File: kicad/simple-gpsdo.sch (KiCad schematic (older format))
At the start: 109 parts, among them J1 PPS_OUT, J10 FAN, J2 PWR, J3 ISP, J4 GPS_NEO, J5 GPS_IN, J6 10MHz_OUT, J7 NEO-6M, J8 10MHz_OUT, J9 USB_C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

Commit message: finalizing revC updates
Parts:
- removed C36: 22uF, Capacitor_SMD:C_1206_3216Metric_Pad1.42x1.75mm_HandSolder, symbol Device:CP_Small
- removed C37: 0.1uF, Capacitor_SMD:C_0805_2012Metric_Pad1.15x1.40mm_HandSolder, symbol Device:C_Small
- removed D6: 1N4148, Diode_SMD:D_SOD-123, symbol Device:D_Small
- removed J10: FAN, Connector_PinHeader_2.54mm:PinHeader_1x02_P2.54mm_Vertical, symbol Connector:Conn_01x02_Female
- removed L4: 3.3uH, Inductor_SMD:L_1206_3216Metric_Pad1.42x1.75mm_HandSolder, symbol Device:L_Small
- removed Q2: PMBT2222, Package_TO_SOT_SMD:SOT-23_Handsoldering, symbol Device:Q_NPN_BEC
- removed R30: 1k, Resistor_SMD:R_0805_2012Metric_Pad1.15x1.40mm_HandSolder, symbol Device:R_Small
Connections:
- net labels removed: FAN_PWM
- wire segments 285 -> 273
- no-connect marks 20 -> 21
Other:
- note removed: "Fan Control"
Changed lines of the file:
@@
 Wire Wire Line
 	7800 4000 7750 4000
-Text Label 4550 5100 1    50   ~ 0
-ADC2
 $Comp
 L Device:R_Small R28
@@
 Text Label 4600 4200 0    50   ~ 0
 ADC2
-$Comp
-L Device:Q_NPN_BEC Q2
-U 1 1 5F768340
-P 1600 7350
-F 0 "Q2" H 1791 7396 50  0000 L CNN
-F 1 "PMBT2222" H 1791 7305 50  0000 L CNN
-F 2 "Package_TO_SOT_SMD:SOT-23_Handsoldering" H 1800 7450 50  0001 C CNN
-F 3 "~" H 1600 7350 50  0001 C CNN
-	1    1600 7350
-	-1   0    0    -1
-$EndComp
-$Comp
-L Device:D_Small D6
-U 1 1 5F785CB2
-P 1500 6950
-F 0 "D6" V 1454 7020 50  0000 L CNN
-F 1 "1N4148" V 1545 7020 50  0000 L CNN
-F 2 "Diode_SMD:D_SOD-123" V 1500 6950 50  0001 C CNN
-F 3 "~" V 1500 6950 50  0001 C CNN
-	1    1500 6950
-	0    1    1    0
-$EndComp
-$Comp
-L Connector:Conn_01x02_Female J10
-U 1 1 5F786D71
-P 1000 7000
-F 0 "J10" H 892 7185 50  0000 C CNN
-F 1 "FAN" H 892 7094 50  0000 C CNN
-F 2 "Connector_PinHeader_2.54mm:PinHeader_1x02_P2.54mm_Vertical" H 1000 7000 50  0001 C CNN
-F 3 "~" H 1000 7000 50  0001 C CNN
-	1    1000 7000
-	-1   0    0    -1
-$EndComp
-$Comp
-L power:GND #PWR066
-U 1 1 5F78873A
-P 1500 7550
-F 0 "#PWR066" H 1500 7300 50  0001 C CNN
-F 1 "GND" H 1505 7377 50  0001 C CNN
-F 2 "" H 1500 7550 50  0001 C CNN
-F 3 "" H 1500 7550 50  0001 C CNN
-	1    1500 7550
-	1    0    0    -1
-$EndComp
-$Comp
-L Device:R_Small R30
-U 1 1 5F78892D
-P 1900 7350
-F 0 "R30" V 2000 7350 50  0000 C BNN
-F 1 "1k" V 1900 7350 40  0000 C CNN
-F 2 "Resistor_SMD:R_0805_2012Metric_Pad1.15x1.40mm_HandSolder" H 1900 7350 50  0001 C CNN
-F 3 "~" H 1900 7350 50  0001 C CNN
-	1    1900 7350
-	0    1    1    0
-$EndComp
-Text GLabel 2100 7450 3    40   Input ~ 0
-FAN_PWM
-Wire Wire Line
-	2100 7350 2000 7350
-$Comp
-L Device:CP_Small C36
-U 1 1 5F7F8DFC
-P 1800 6850
-F 0 "C36" H 1888 6896 50  0000 L CNN
-F 1 "22uF" H 1888 6805 50  0000 L CNN
-F 2 "Capacitor_SMD:C_1206_3216Metric_Pad1.42x1.75mm_HandSolder" H 1800 6850 50  0001 C CNN
-F 3 "~" H 1800 6850 50  0001 C CNN
-	1    1800 6850
-	1    0    0    -1
-$EndComp
-Wire Wire Line
-	2100 7350 2100 7450
-$Comp
-L power:GND #PWR067
-U 1 1 5F8108C5
-P 1800 6950
-F 0 "#PWR067" H 1800 6700 50  0001 C CNN
-F 1 "GND" H 1805 6777 50  0001 C CNN
-F 2 "" H 1800 6950 50  0001 C CNN
-F 3 "" H 1800 6950 50  0001 C CNN
-	1    1800 6950
-	1    0    0    -1
-$EndComp
-$Comp
-L Device:C_Small C37
-U 1 1 5F810BCA
-P 2150 6850
-F 0 "C37" V 1921 6850 50  0000 C CNN
-F 1 "0.1uF" V 2012 6850 50  0000 C CNN
-F 2 "Capacitor_SMD:C_0805_2012Metric_Pad1.15x1.40mm_HandSolder" H 2150 6850 50  0001 C CNN
-F 3 "~" H 2150 6850 50  0001 C CNN
-	1    2150 6850
-	-1   0    0    -1
-$EndComp
-$Comp
-L power:GND #PWR068
-U 1 1 5F81112D
-P 2150 6950
-F 0 "#PWR068" H 2150 6700 50  0001 C CNN
-F 1 "GND" H 2155 6777 50  0001 C CNN
-F 2 "" H 2150 6950 50  0001 C CNN
-F 3 "" H 2150 6950 50  0001 C CNN
-	1    2150 6950
-	1    0    0    -1
-$EndComp
-Wire Wire Line
-	1200 7000 1350 7000
-Wire Wire Line
-	2150 6700 2150 6750
-$Comp
-L power:+5VD #PWR065
-U 1 1 5F858FD4
-P 1350 6450
-F 0 "#PWR065" H 1350 6300 50  0001 C CNN
-F 1 "+5VD" H 1365 6623 50  0000 C CNN
-F 2 "" H 1350 6450 50  0001 C CNN
-F 3 "" H 1350 6450 50  0001 C CNN
-	1    1350 6450
-	1    0    0    -1
-$EndComp
-$Comp
-L Device:L_Small L4
-U 1 1 5F859F8F
-P 1350 6550
-F 0 "L4" H 1398 6596 50  0000 L CNN
-F 1 "3.3uH" H 1398 6505 50  0000 L CNN
-F 2 "Inductor_SMD:L_1206_3216Metric_Pad1.42x1.75mm_HandSolder" H 1350 6550 50  0001 C CNN
-F 3 "~" H 1350 6550 50  0001 C CNN
-	1    1350 6550
-	-1   0    0    -1
-$EndComp
-Wire Wire Line
-	2150 6700 1800 6700
-Wire Wire Line
-	1500 6850 1500 6700
-Wire Wire Line
-	1800 6750 1800 6700
-Connection ~ 1800 6700
-Wire Wire Line
-	1800 6700 1500 6700
-Wire Wire Line
-	1350 6650 1350 7000
-Wire Wire Line
-	1500 7050 1500 7100
-Wire Wire Line
-	1200 7100 1500 7100
-Connection ~ 1500 7100
-Wire Wire Line
-	1500 7100 1500 7150
-Text Notes 1500 6600 0    50   ~ 0
-Fan Control
-Text GLabel 2650 4850 3    40   Input ~ 0
-FAN_PWM
-Text GLabel 4100 3400 2    50   Input ~ 0
-FAN_PWM
+NoConn ~ 4100 3400
 $EndSCHEMATC

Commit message: schematic cleanup and re-plot of gerber files
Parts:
- J9: symbol Connector:USB_C_Receptacle_USB2.0 -> simple-gpsdo-rescue:USB_C_Receptacle_USB2.0-Connector
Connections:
- no-connect marks 21 -> 20
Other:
- moved on the sheet: C1, C2, Y1
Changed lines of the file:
@@
 Connection ~ 2800 1150
-$Comp
-L Device:C_Small C2
-U 1 1 5F6D722A
-P 2250 3950
-F 0 "C2" H 2158 3904 50  0000 R CNN
-F 1 "6.8pF" H 2158 3995 50  0000 R CNN
-F 2 "Capacitor_SMD:C_0805_2012Metric_Pad1.15x1.40mm_HandSolder" H 2250 3950 50  0001 C CNN
-F 3 "~" H 2250 3950 50  0001 C CNN
-	1    2250 3950
-	0    -1   -1   0
-$EndComp
-$Comp
-L Device:C_Small C1
-U 1 1 5F6DDEED
-P 2250 3450
-F 0 "C1" H 2159 3404 50  0000 R CNN
-F 1 "6.8pF" H 2159 3495 50  0000 R CNN
-F 2 "Capacitor_SMD:C_0805_2012Metric_Pad1.15x1.40mm_HandSolder" H 2250 3450 50  0001 C CNN
-F 3 "~" H 2250 3450 50  0001 C CNN
-	1    2250 3450
-	0    -1   1    0
-$EndComp
 $Comp
 L Device:C_Small C4
@@
 F 3 "~" H 1550 1250 50  0001 C CNN
 	1    1550 1250
-	1    0    0    -1
+	-1   0    0    -1
 $EndComp
 Wire Wire Line
@@
 $EndComp
 $Comp
-L Connector:USB_C_Receptacle_USB2.0 J9
+L simple-gpsdo-rescue:USB_C_Receptacle_USB2.0-Connector J9
 U 1 1 5F73B888
 P 1300 2600
@@
 NoConn ~ 1900 2300
 NoConn ~ 2850 2150
-NoConn ~ 1250 800
-$Comp
-L Device:Crystal_GND24 Y1
-U 1 1 5F750A50
-P 2400 3700
-F 0 "Y1" V 2150 3600 50  0000 R CNN
-F 1 "16MHz" V 2250 3600 50  0000 R CNN
-F 2 "Crystal:Crystal_SMD_SeikoEpson_TSX3225-4Pin_3.2x2.5mm_HandSoldering" H 2400 3700 50  0001 C CNN
-F 3 "~" H 2400 3700 50  0001 C CNN
-	1    2400 3700
-	0    -1   1    0
-$EndComp
 Wire Wire Line
 	1600 3950 1600 3850
@@
 	1    0    0    -1
 $EndComp
-$Comp
-L power:GND #PWR03
-U 1 1 5F85D4E9
-P 2100 4050
-F 0 "#PWR03" H 2100 3800 50  0001 C CNN
-F 1 "GND" H 2105 3877 50  0001 C CNN
-F 2 "" H 2100 4050 50  0001 C CNN
-F 3 "" H 2100 4050 50  0001 C CNN
-	1    2100 4050
-	1    0    0    -1
-$EndComp
-$Comp
-L power:GND #PWR07
-U 1 1 5F85DF21
-P 2650 3750
-F 0 "#PWR07" H 2650 3500 50  0001 C CNN
-F 1 "GND" H 2655 3577 50  0001 C CNN
-F 2 "" H 2650 3750 50  0001 C CNN
-F 3 "" H 2650 3750 50  0001 C CNN
-	1    2650 3750
-	1    0    0    -1
-$EndComp
-Wire Wire Line
-	2600 3700 2650 3700
-Wire Wire Line
-	2500 3700 2500 3750
-Wire Wire Line
-	2350 3450 2400 3450
-Wire Wire Line
-	2400 3450 2400 3550
-Wire Wire Line
-	2150 3450 2100 3450
-Wire Wire Line
-	2100 3450 2100 3700
-Wire Wire Line
-	2150 3950 2100 3950
-Connection ~ 2100 3950
-Wire Wire Line
-	2100 3950 2100 4050
-Wire Wire Line
-	2200 3700 2100 3700
-Connection ~ 2100 3700
-Wire Wire Line
-	2100 3700 2100 3950
-Wire Wire Line
-	2350 3950 2400 3950
-Wire Wire Line
-	2400 3950 2400 3850
 Text GLabel 2700 1700 0    50   Input ~ 0
 XTAL1
@@
 Wire Wire Line
 	2700 1900 2900 1900
-Text GLabel 2400 3350 1    50   Input ~ 0
-XTAL1
-Wire Wire Line
-	2400 3350 2400 3450
-Connection ~ 2400 3450
-Text GLabel 2400 4050 3    50   Input ~ 0
-XTAL2
-Wire Wire Line
-	2400 3950 2400 4050
-Connection ~ 2400 3950
-Wire Wire Line
-	2650 3750 2650 3700
+Wire Wire Line
+	2850 4000 2850 3950
 Wire Wire Line
 	4100 2200 4900 2200
@@
 ADC2
 NoConn ~ 4100 3400
+Connection ~ 2600 4200
+Wire Wire Line
+	2600 4200 2600 4300
+Text GLabel 2600 4300 3    50   Input ~ 0
+XTAL2
+Connection ~ 2600 3700
+Wire Wire Line
+	2600 3600 2600 3700
+Text GLabel 2600 3600 1    50   Input ~ 0
+XTAL1
+Wire Wire Line
+	2600 4200 2600 4100
+Wire Wire Line
+	2550 4200 2600 4200
+Wire Wire Line
+	2300 3950 2300 4200
+Connection ~ 2300 3950
+Wire Wire Line
+	2400 3950 2300 3950
+Wire Wire Line
+	2300 4200 2300 4300
+Connection ~ 2300 4200
+Wire Wire Line
+	2350 4200 2300 4200
+Wire Wire Line
+	2300 3700 2300 3950
+Wire Wire Line
+	2350 3700 2300 3700
+Wire Wire Line
+	2600 3700 2600 3800
+Wire Wire Line
+	2550 3700 2600 3700
+Wire Wire Line
+	2700 3950 2700 4000
+Wire Wire Line
+	2800 3950 2850 3950
+$Comp
+L power:GND #PWR07
+U 1 1 5F85DF21
+P 2850 4000
+F 0 "#PWR07" H 2850 3750 50  0001 C CNN
+F 1 "GND" H 2855 3827 50  0001 C CNN
+F 2 "" H 2850 4000 50  0001 C CNN
+F 3 "" H 2850 4000 50  0001 C CNN
+	1    2850 4000
+	1    0    0    -1
+$EndComp
+$Comp
+L power:GND #PWR03
+U 1 1 5F85D4E9
+P 2300 4300
+F 0 "#PWR03" H 2300 4050 50  0001 C CNN
+F 1 "GND" H 2305 4127 50  0001 C CNN
+F 2 "" H 2300 4300 50  0001 C CNN
+F 3 "" H 2300 4300 50  0001 C CNN
+	1    2300 4300
+	1    0    0    -1
+$EndComp
+$Comp
+L Device:Crystal_GND24 Y1
+U 1 1 5F750A50
+P 2600 3950
+F 0 "Y1" V 2350 3850 50  0000 R CNN
+F 1 "16MHz" V 2450 3850 50  0000 R CNN
+F 2 "Crystal:Crystal_SMD_SeikoEpson_TSX3225-4Pin_3.2x2.5mm_HandSoldering" H 2600 3950 50  0001 C CNN
+F 3 "~" H 2600 3950 50  0001 C CNN
+	1    2600 3950
+	0    -1   1    0
+$EndComp
+$Comp
+L Device:C_Small C1
+U 1 1 5F6DDEED
+P 2450 3700
+F 0 "C1" H 2359 3654 50  0000 R CNN
+F 1 "6.8pF" H 2359 3745 50  0000 R CNN
+F 2 "Capacitor_SMD:C_0805_2012Metric_Pad1.15x1.40mm_HandSolder" H 2450 3700 50  0001 C CNN
+F 3 "~" H 2450 3700 50  0001 C CNN
+	1    2450 3700
+	0    -1   1    0
+$EndComp
+$Comp
+L Device:C_Small C2
+U 1 1 5F6D722A
+P 2450 4200
+F 0 "C2" H 2358 4154 50  0000 R CNN
+F 1 "6.8pF" H 2358 4245 50  0000 R CNN
+F 2 "Capacitor_SMD:C_0805_2012Metric_Pad1.15x1.40mm_HandSolder" H 2450 4200 50  0001 C CNN
+F 3 "~" H 2450 4200 50  0001 C CNN
+	1    2450 4200
+	0    -1   -1   0
+$EndComp
 $EndSCHEMATC

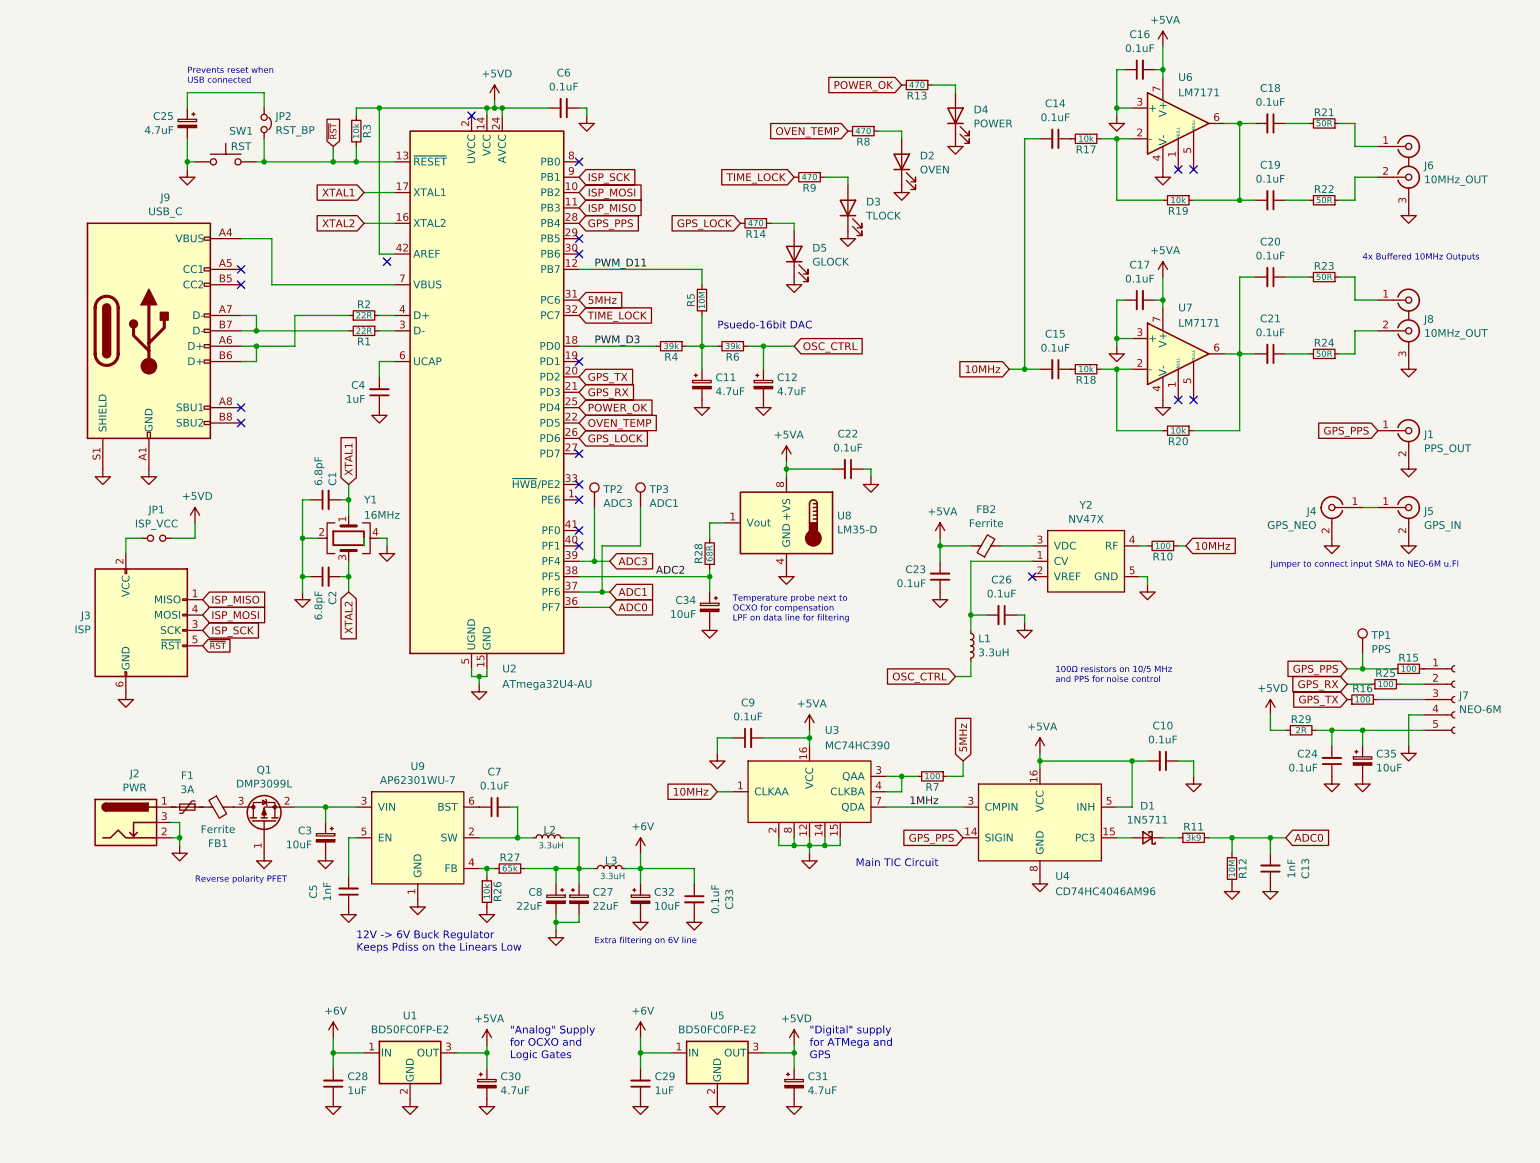
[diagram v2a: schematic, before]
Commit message: finalized simple schematic, started PCB rework
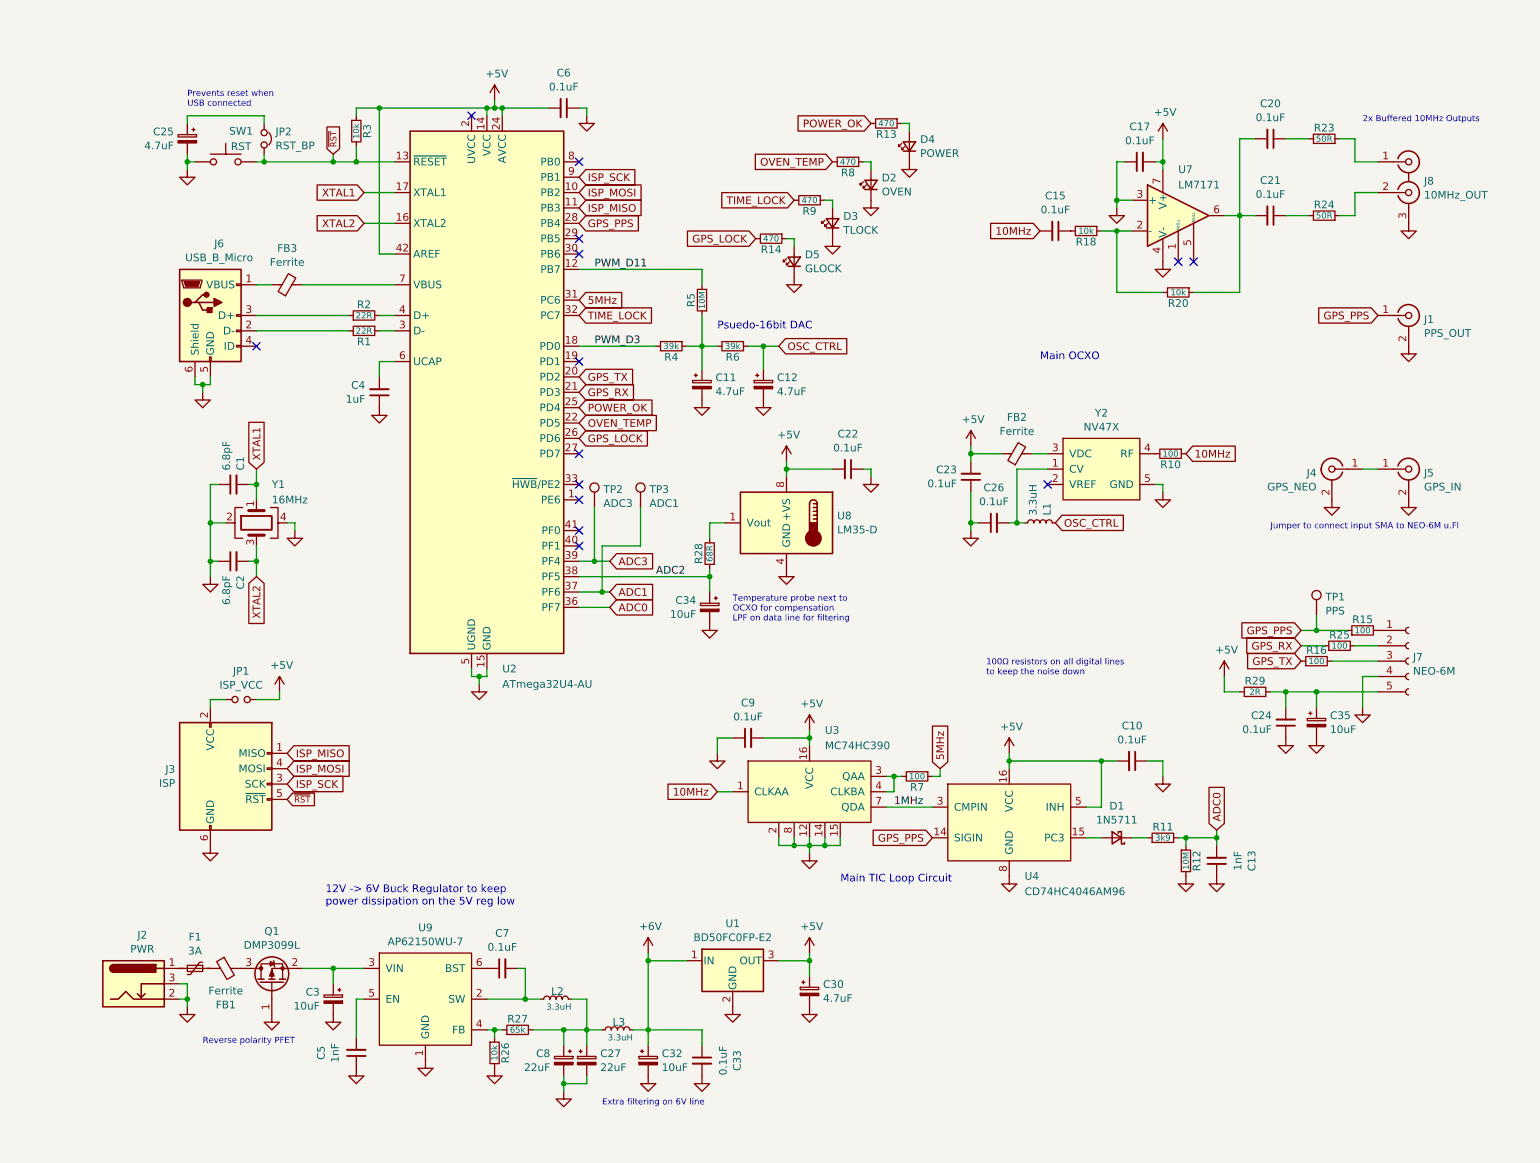
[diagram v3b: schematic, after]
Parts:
- removed C14, C16, C18, C19: 0.1uF, Capacitor_SMD:C_0805_2012Metric_Pad1.15x1.40mm_HandSolder, symbol Device:C_Small
- removed C28, C29: 1uF, Capacitor_SMD:C_0805_2012Metric_Pad1.15x1.40mm_HandSolder, symbol Device:C_Small
- removed C31: 4.7uF, Capacitor_SMD:C_1206_3216Metric_Pad1.42x1.75mm_HandSolder, symbol Device:CP_Small
- removed D2: OVEN, LED_SMD:LED_1206_3216Metric_Pad1.42x1.75mm_HandSolder, symbol Device:LED
- removed D3: TLOCK, LED_SMD:LED_1206_3216Metric_Pad1.42x1.75mm_HandSolder, symbol Device:LED
- removed D4: POWER, LED_SMD:LED_1206_3216Metric_Pad1.42x1.75mm_HandSolder, symbol Device:LED
- removed D5: GLOCK, LED_SMD:LED_1206_3216Metric_Pad1.42x1.75mm_HandSolder, symbol Device:LED
- removed J6: 10MHz_OUT, molex:734152980, symbol Connector:Conn_Coaxial_x2
- removed J9: USB_C, Kycon:KUSBX-SL-CS1N14-B, symbol simple-gpsdo-rescue:USB_C_Receptacle_USB2.0-Connector
- removed R17, R19: 10k, Resistor_SMD:R_0805_2012Metric_Pad1.15x1.40mm_HandSolder, symbol Device:R_Small
- removed R21, R22: 50R, Resistor_SMD:R_0805_2012Metric_Pad1.15x1.40mm_HandSolder, symbol Device:R_Small
- removed U5: BD50FC0FP-E2, Package_TO_SOT_SMD:TO-252-2, symbol Regulator_Linear:L7805
- removed U6: LM7171, Package_SO:SOIC-8_3.9x4.9mm_P1.27mm, symbol Amplifier_Operational:AD8610
- added D2: OVEN, LED_THT:LED_D3.0mm_Horizontal_O1.27mm_Z2.0mm_Clear, symbol Device:LED_Small
- added D3: TLOCK, LED_THT:LED_D3.0mm_Horizontal_O1.27mm_Z2.0mm_Clear, symbol Device:LED_Small
- added D4: POWER, LED_THT:LED_D3.0mm_Horizontal_O1.27mm_Z2.0mm_Clear, symbol Device:LED_Small
- added D5: GLOCK, LED_THT:LED_D3.0mm_Horizontal_O1.27mm_Z2.0mm_Clear, symbol Device:LED_Small
- added FB3: Ferrite, Fuse:Fuse_1206_3216Metric_Pad1.42x1.75mm_HandSolder, symbol Device:Ferrite_Bead_Small
- added J6: USB_B_Micro, Connector_USB:USB_Mini-B_Wuerth_65100516121_Horizontal, symbol Connector:USB_B_Micro
- U9: value AP62301WU-7 -> AP62150WU-7
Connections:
- net +5VD is gone; now on net +5V: C6.2, JP1.2, R29.1, R3.1, U2.14 (VCC), U2.24 (AVCC), U2.34 (VCC), U2.42 (AREF), U2.44 (AVCC)
- net GND: now also D2.1 (K), D3.1 (K), D4.1 (K), D5.1 (K), J6.5 (GND), J6.6 (Shield)
- net OSC_CTRL: now also L1.1; no longer L1.2
- net at U2.7 (VBUS): now also FB3.2
- net at R2.1: now also J6.3 (D+)
- net at R1.2: now also J6.2 (D-)
- net at R13.1: now also D4.2 (A)
- net at R8.1: now also D2.2 (A)
- net at R14.1: now also D5.2 (A)
- net at R9.1: now also D3.2 (A)
- net at C26.2, Y2.1 (CV): now also L1.2; no longer L1.1
- net +5VA renamed +5V
- new net: FB3.1, J6.1 (VBUS)
- no-connect marks 20 -> 14
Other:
- note added: "100Ω resistors on all digital lines\nto keep the noise down"
- note added: "12V -> 6V Buck Regulator to keep\npower dissipation on the 5V reg low"
- note added: "2x Buffered 10MHz Outputs"
- note added: "Main OCXO"
- note added: "Main TIC Loop Circuit"
- note removed: ""Analog" Supply \nfor OCXO and\nLogic Gates"
- note removed: ""Digital" supply\nfor ATMega and \nGPS"
- note removed: "100Ω resistors on 10/5 MHz\nand PPS for noise control"
- note removed: "12V -> 6V Buck Regulator\nKeeps Pdiss on the Linears Low"
- note removed: "4x Buffered 10MHz Outputs"
- note removed: "Main TIC Circuit"
- moved on the sheet: C1, C10, C13, C15, C17, C2, C20, C21, C23, C24, C25, C26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

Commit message: finalized new schematic and board
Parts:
- removed J4: GPS_NEO, Connector_Coaxial:U.FL_Hirose_U.FL-R-SMT-1_Vertical, symbol Connector:Conn_Coaxial
- removed J5: GPS_IN, Connector_Coaxial:SMA_Amphenol_132203-12_Horizontal, symbol Connector:Conn_Coaxial
- added D6: PPS, LED_THT:LED_D3.0mm_Horizontal_O1.27mm_Z2.0mm_Clear, symbol Device:LED_Small
- added R17: 470, Resistor_SMD:R_0805_2012Metric_Pad1.15x1.40mm_HandSolder, symbol Device:R_Small
- SW1: footprint Button_Switch_SMD:SW_SPST_PTS645 -> Connector_PinHeader_2.54mm:PinHeader_1x02_P2.54mm_Vertical
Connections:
- net GND: now also D6.1 (K)
- net GPS_PPS: now also R17.2
- new net: D6.2 (A), R17.1
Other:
- note added: "GPS ANT connects to module\nvia SMA-u.FL bulkhead & jumper"
- note added: "PPS connection is a jumper\nto bulkhead SMA"
- note removed: "Jumper to connect input SMA to NEO-6M u.Fl"
- moved on the sheet: D2, D3, D4, D5, R13, R14, R8, R9
